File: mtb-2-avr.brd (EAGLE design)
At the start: 27 x 22 mm, 18 parts, among them IC1 MEGA8A-AU, Q1/2 14.745 MHz, Q2 14.745 MHz

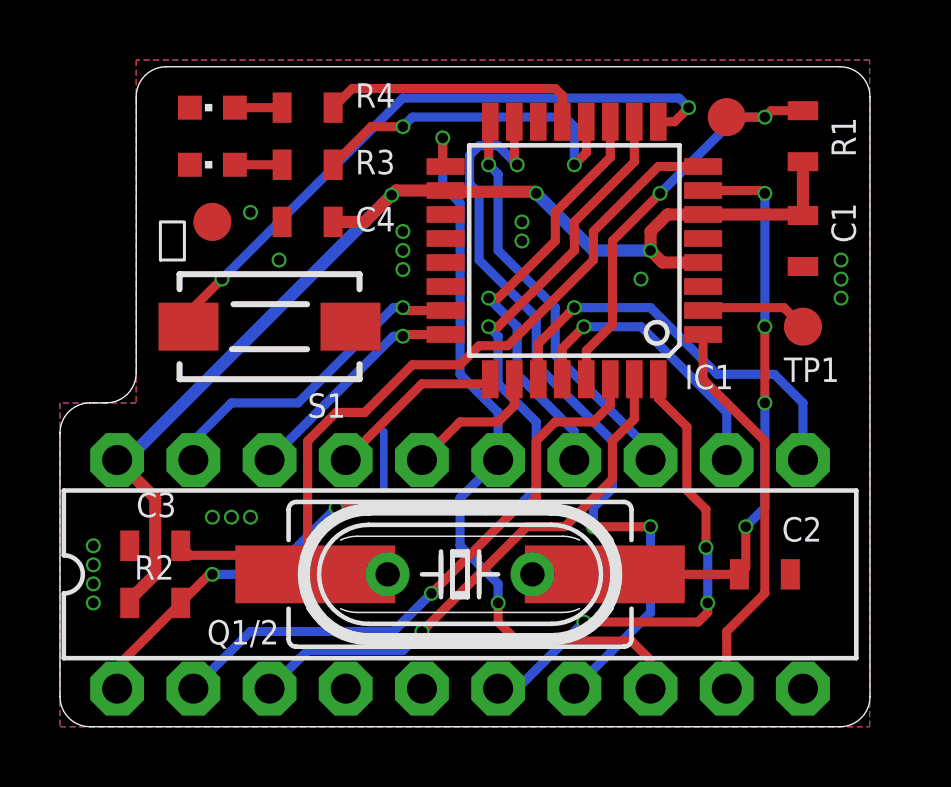
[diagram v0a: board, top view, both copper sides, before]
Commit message: Add pull-up on TX_OE.
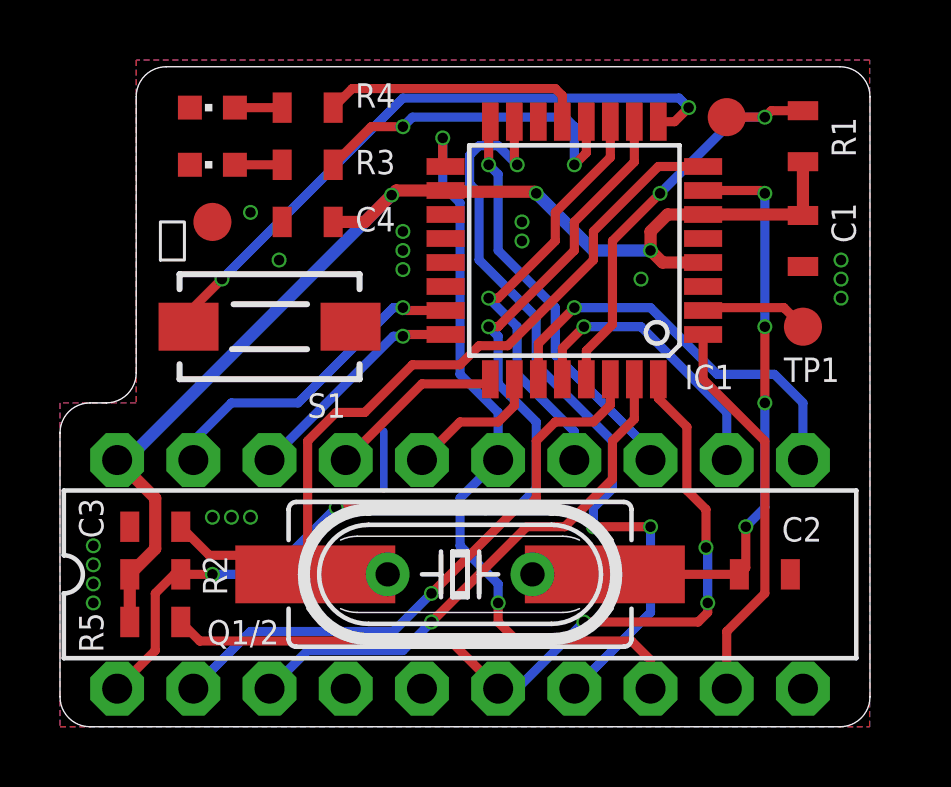
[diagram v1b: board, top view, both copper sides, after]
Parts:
- added R5: 100k, rcl:R0603
- moved R2 0.95 mm to (3.17, 5.08)
- moved C3 0.64 mm to (3.17, 6.67)
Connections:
- net TX_OE: now also R5.1
- net VCC: now also R5.2
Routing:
- net TX_OE: track 16.5 -> 28.0 mm
- net !SHIFT_OE: track 32.2 -> 32.9 mm
- net VCC: track 40.0 -> 40.6 mm
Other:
- board text added: "v1.2 JH 2021"
- board text removed: "v1.1 JH 2021"
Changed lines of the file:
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@@
 <text x="6.985" y="18.0975" size="1.016" layer="22" rot="MR0" align="bottom-center">MTB-UNI
 v2 upgrade</text>
-<text x="24.4475" y="16.51" size="1.016" layer="22" rot="MR90" align="bottom-center">v1.1 JH 2021</text>
+<text x="24.4475" y="16.51" size="1.016" layer="22" rot="MR90" align="bottom-center">v1.2 JH 2021</text>
 <text x="24.765" y="2.54" size="1.27" layer="22" rot="MR90" align="center-left">⏚</text>
 <text x="17.145" y="2.54" size="1.27" layer="22" rot="MR90" align="center-left">MOSI</text>
@@
 <attribute name="VALUE" x="24.765" y="4.1275" size="0.8128" layer="27" rot="R180"/>
 </element>
-<element name="C3" library="rcl" package="C0603" value="22p" x="3.175" y="6.0325" smashed="yes">
-<attribute name="LCSC_PART" value="C1653" x="3.175" y="6.0325" size="1.778" layer="27" display="off"/>
-<attribute name="NAME" x="2.54" y="6.985" size="0.8128" layer="25"/>
-<attribute name="VALUE" x="4.445" y="5.715" size="0.8128" layer="27"/>
+<element name="C3" library="rcl" package="C0603" value="22p" x="3.175" y="6.6675" smashed="yes">
+<attribute name="LCSC_PART" value="C1653" x="3.175" y="6.6675" size="1.778" layer="27" display="off"/>
+<attribute name="NAME" x="0.635" y="7.62" size="0.8128" layer="25" rot="R270"/>
+<attribute name="VALUE" x="4.445" y="6.35" size="0.8128" layer="27"/>
 </element>
 <element name="C4" library="rcl" package="C0603" value="100n" x="8.255" y="16.8275" smashed="yes" rot="R180">
@@
 <attribute name="VALUE" x="6.985" y="17.145" size="0.8128" layer="27" rot="R180"/>
 </element>
-<element name="R2" library="rcl" package="R0603" value="10k" x="3.175" y="4.1275" smashed="yes" rot="R180">
-<attribute name="LCSC_PART" value="C25804" x="3.175" y="4.1275" size="1.778" layer="27" rot="R180" display="off"/>
-<attribute name="NAME" x="3.81" y="5.715" size="0.8128" layer="25" rot="R180"/>
-<attribute name="VALUE" x="1.905" y="4.445" size="0.8128" layer="27" rot="R180"/>
+<element name="R2" library="rcl" package="R0603" value="10k" x="3.175" y="5.08" smashed="yes" rot="R180">
+<attribute name="LCSC_PART" value="C25804" x="3.175" y="5.08" size="1.778" layer="27" rot="R180" display="off"/>
+<attribute name="NAME" x="4.7625" y="5.715" size="0.8128" layer="25" rot="R270"/>
+<attribute name="VALUE" x="1.905" y="5.3975" size="0.8128" layer="27" rot="R180"/>
 </element>
 <element name="R3" library="rcl" package="R0603" value="10k" x="8.255" y="18.7325" smashed="yes">
@@
 <attribute name="OC_NEWARK" value="unknown" x="13.335" y="5.08" size="1.778" layer="27" display="off"/>
 <attribute name="POPULARITY" value="49" x="13.335" y="5.08" size="1.778" layer="27" display="off"/>
-<attribute name="VALUE" x="8.255" y="1.143" size="1.27" layer="27" ratio="10"/>
+</element>
+<element name="R5" library="rcl" package="R0603" value="100k" x="3.175" y="3.4925" smashed="yes" rot="R180">
+<attribute name="LCSC_PART" value="C25803" x="3.175" y="3.4925" size="1.778" layer="27" rot="R180" display="off"/>
+<attribute name="NAME" x="0.635" y="3.81" size="0.8128" layer="25" rot="R270"/>
+<attribute name="VALUE" x="4.445" y="3.175" size="0.8128" layer="27"/>
 </element>
 </elements>
@@
 <wire x1="17.78" y1="15.875" x2="15.875" y2="17.78" width="0.4064" layer="16"/>
 <wire x1="19.685" y1="15.875" x2="17.78" y2="15.875" width="0.4064" layer="16"/>
-<wire x1="3.175" y1="5.08" x2="2.325" y2="4.23" width="0.4064" layer="1"/>
-<wire x1="2.325" y1="4.23" x2="2.325" y2="4.1275" width="0.4064" layer="1"/>
-<wire x1="3.175" y1="7.62" x2="3.175" y2="5.08" width="0.4064" layer="1"/>
+<wire x1="3.175" y1="5.93" x2="2.325" y2="5.08" width="0.4064" layer="1"/>
+<wire x1="3.175" y1="7.62" x2="3.175" y2="5.93" width="0.4064" layer="1"/>
 <wire x1="24.765" y1="18.835" x2="24.765" y2="17.0425" width="0.4064" layer="1"/>
 <via x="11.05480625" y="17.72230625" extent="1-16" drill="0.35"/>
@@
 <wire x1="9.105" y1="16.8275" x2="10.16" y2="16.8275" width="0.4064" layer="1"/>
 <wire x1="10.16" y1="16.8275" x2="11.05480625" y2="17.72230625" width="0.4064" layer="1"/>
+<contactref element="R5" pad="2"/>
+<wire x1="2.325" y1="3.4925" x2="2.325" y2="5.08" width="0.4064" layer="1"/>
 </signal>
 <signal name="RXD">
@@
 <wire x1="6.985" y1="1.27" x2="8.255" y2="2.54" width="0.3048" layer="16"/>
 <wire x1="8.255" y1="2.54" x2="11.43" y2="2.54" width="0.3048" layer="16"/>
-<wire x1="11.43" y1="2.54" x2="12.065" y2="3.175" width="0.3048" layer="16"/>
-<wire x1="15.5575" y1="6.6675" x2="12.065" y2="3.175" width="0.3048" layer="1"/>
-<via x="12.065" y="3.175" extent="1-16" drill="0.35"/>
+<wire x1="11.43" y1="2.54" x2="12.3825" y2="3.4925" width="0.3048" layer="16"/>
+<wire x1="15.5575" y1="6.6675" x2="12.3825" y2="3.4925" width="0.3048" layer="1"/>
+<via x="12.3825" y="3.4925" extent="1-16" drill="0.35"/>
 <wire x1="16.8275" y1="6.6675" x2="15.5575" y2="6.6675" width="0.3048" layer="1"/>
 </signal>
@@
 <wire x1="17.4625" y1="3.4925" x2="15.24" y2="1.27" width="0.3048" layer="16"/>
 <via x="17.4625" y="3.4925" extent="1-16" drill="0.35"/>
+<contactref element="R5" pad="1"/>
+<wire x1="14.605" y1="1.27" x2="13.0175" y2="2.8575" width="0.3048" layer="1"/>
+<wire x1="4.66" y1="2.8575" x2="4.025" y2="3.4925" width="0.3048" layer="1"/>
+<wire x1="13.0175" y1="2.8575" x2="4.66" y2="2.8575" width="0.3048" layer="1"/>
 </signal>
 <signal name="OUT_SET">
@@
 <wire x1="8.255" y1="5.334" x2="8.255" y2="9.525" width="0.3048" layer="1"/>
 <wire x1="11.7475" y1="12.065" x2="13.335" y2="12.065" width="0.3048" layer="1"/>
-<wire x1="4.3425" y1="5.715" x2="4.025" y2="6.0325" width="0.3048" layer="1"/>
-<wire x1="7.874" y1="5.715" x2="4.3425" y2="5.715" width="0.3048" layer="1"/>
+<wire x1="4.9775" y1="5.715" x2="4.025" y2="6.6675" width="0.3048" layer="1"/>
+<wire x1="7.874" y1="5.715" x2="4.9775" y2="5.715" width="0.3048" layer="1"/>
 <wire x1="21.4376" y1="18.675" x2="19.945" y2="18.675" width="0.3048" layer="1"/>
 <wire x1="19.945" y1="18.675" x2="17.78" y2="16.51" width="0.3048" layer="1"/>
@@
 <wire x1="14.1831" y1="7.3025" x2="9.2075" y2="7.3025" width="0.3048" layer="1"/>
 <wire x1="15.24" y1="7.3025" x2="14.1831" y2="7.3025" width="0.3048" layer="16"/>
-<wire x1="1.905" y1="1.27" x2="1.905" y2="2.0075" width="0.3048" layer="1"/>
-<wire x1="1.905" y1="2.0075" x2="4.025" y2="4.1275" width="0.3048" layer="1"/>
 <via x="9.2075" y="7.3025" extent="1-16" drill="0.35"/>
 <wire x1="9.2075" y1="7.3025" x2="6.985" y2="5.08" width="0.3048" layer="16"/>
 <wire x1="6.985" y1="5.08" x2="5.08" y2="5.08" width="0.3048" layer="16"/>
 <via x="5.08" y="5.08" extent="1-16" drill="0.35"/>
-<wire x1="5.08" y1="5.08" x2="4.9775" y2="5.08" width="0.3048" layer="1"/>
-<wire x1="4.9775" y1="5.08" x2="4.025" y2="4.1275" width="0.3048" layer="1"/>
+<wire x1="5.08" y1="5.08" x2="4.025" y2="5.08" width="0.3048" layer="1"/>
+<wire x1="1.905" y1="1.27" x2="3.175" y2="2.54" width="0.3048" layer="1"/>
+<wire x1="3.175" y1="2.54" x2="3.175" y2="4.445" width="0.3048" layer="1"/>
+<wire x1="3.175" y1="4.445" x2="3.81" y2="5.08" width="0.3048" layer="1"/>
+<wire x1="3.81" y1="5.08" x2="4.025" y2="5.08" width="0.3048" layer="1"/>
 </signal>
 <signal name="N$3">

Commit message: Minor tweaks of wire positions.
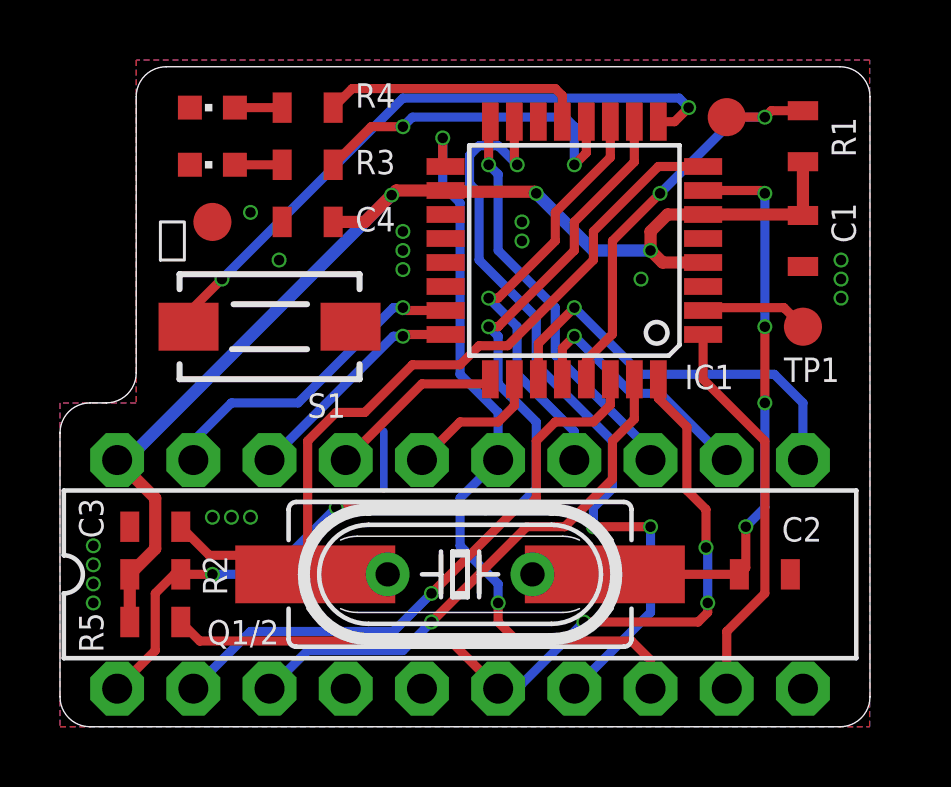
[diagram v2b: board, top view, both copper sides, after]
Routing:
- net SCL: track 9.58 -> 8.39 mm
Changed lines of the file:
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@@
 <wire x1="24.765" y1="8.89" x2="24.765" y2="10.795" width="0.3048" layer="16"/>
 <wire x1="24.765" y1="10.795" x2="23.8125" y2="11.7475" width="0.3048" layer="16"/>
-<wire x1="23.8125" y1="11.7475" x2="21.9075" y2="11.7475" width="0.3048" layer="16"/>
-<wire x1="21.9075" y1="11.7475" x2="19.685" y2="13.97" width="0.3048" layer="16"/>
-<wire x1="19.685" y1="13.97" x2="17.145" y2="13.97" width="0.3048" layer="16"/>
+<wire x1="23.8125" y1="11.7475" x2="19.3675" y2="11.7475" width="0.3048" layer="16"/>
+<wire x1="19.3675" y1="11.7475" x2="17.145" y2="13.97" width="0.3048" layer="16"/>
 <wire x1="15.945" y1="11.5824" x2="15.945" y2="12.77" width="0.3048" layer="1"/>
 <wire x1="15.945" y1="12.77" x2="17.145" y2="13.97" width="0.3048" layer="1"/>
@@
 <contactref element="IC1" pad="28"/>
 <wire x1="16.745" y1="11.5824" x2="16.745" y2="12.6175" width="0.3048" layer="1"/>
-<wire x1="16.745" y1="12.6175" x2="17.4625" y2="13.335" width="0.3048" layer="1"/>
-<wire x1="22.225" y1="8.89" x2="22.225" y2="10.4775" width="0.3048" layer="16"/>
-<wire x1="22.225" y1="10.4775" x2="19.3675" y2="13.335" width="0.3048" layer="16"/>
-<wire x1="19.3675" y1="13.335" x2="17.4625" y2="13.335" width="0.3048" layer="16"/>
-<via x="17.4625" y="13.335" extent="1-16" drill="0.35"/>
+<wire x1="16.745" y1="12.6175" x2="17.145" y2="13.0175" width="0.3048" layer="1"/>
+<via x="17.145" y="13.0175" extent="1-16" drill="0.35"/>
+<wire x1="17.145" y1="13.0175" x2="19.05" y2="11.1125" width="0.3048" layer="16"/>
+<wire x1="19.05" y1="11.1125" x2="20.0025" y2="11.1125" width="0.3048" layer="16"/>
+<wire x1="20.0025" y1="11.1125" x2="22.225" y2="8.89" width="0.3048" layer="16"/>
 </signal>
 <signal name="CRYST+">
@@
 <contactref element="IC1" pad="29"/>
 <contactref element="R1" pad="1"/>
-<wire x1="17.545" y1="11.5824" x2="17.545" y2="12.5349" width="0.3048" layer="1"/>
-<wire x1="18.415" y1="13.4049" x2="17.545" y2="12.5349" width="0.3048" layer="1"/>
+<wire x1="17.545" y1="11.5824" x2="17.545" y2="12.2174" width="0.3048" layer="1"/>
+<wire x1="18.415" y1="13.0874" x2="17.545" y2="12.2174" width="0.3048" layer="1"/>
 <wire x1="20.0025" y1="17.78" x2="18.415" y2="16.1925" width="0.3048" layer="1"/>
-<wire x1="18.415" y1="16.1925" x2="18.415" y2="13.4049" width="0.3048" layer="1"/>
+<wire x1="18.415" y1="16.1925" x2="18.415" y2="13.0874" width="0.3048" layer="1"/>
 <via x="20.0025" y="17.78" extent="1-16" drill="0.35"/>
 <wire x1="20.0025" y1="17.78" x2="22.5425" y2="20.32" width="0.3048" layer="16"/>

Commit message: Use ATmega328.
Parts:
- IC1: value MEGA8A-AU -> MEGA328A-AU
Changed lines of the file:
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@@
 </autorouter>
 <elements>
-<element name="IC1" library="atmel" library_urn="urn:adsk.eagle:library:105" package="TQFP32-08" package3d_urn="urn:adsk.eagle:package:4313/2" value="MEGA8A-AU" x="17.145" y="15.875" smashed="yes" rot="R180">
-<attribute name="LCSC_PART" value="C16190" x="17.145" y="15.875" size="1.778" layer="27" rot="R180" display="off"/>
+<element name="IC1" library="atmel" library_urn="urn:adsk.eagle:library:105" package="TQFP32-08" package3d_urn="urn:adsk.eagle:package:4313/2" value="MEGA328A-AU" x="17.145" y="15.875" smashed="yes" rot="R180">
+<attribute name="LCSC_PART" value="C14877" x="17.145" y="15.875" size="1.778" layer="27" rot="R180" display="off"/>
 <attribute name="MF" value="" x="-0.635" y="20.955" size="1.778" layer="27" rot="R180" display="off"/>
 <attribute name="MPN" value="ATMEGA8-16AU" x="-0.635" y="20.955" size="1.778" layer="27" rot="R180" display="off"/>

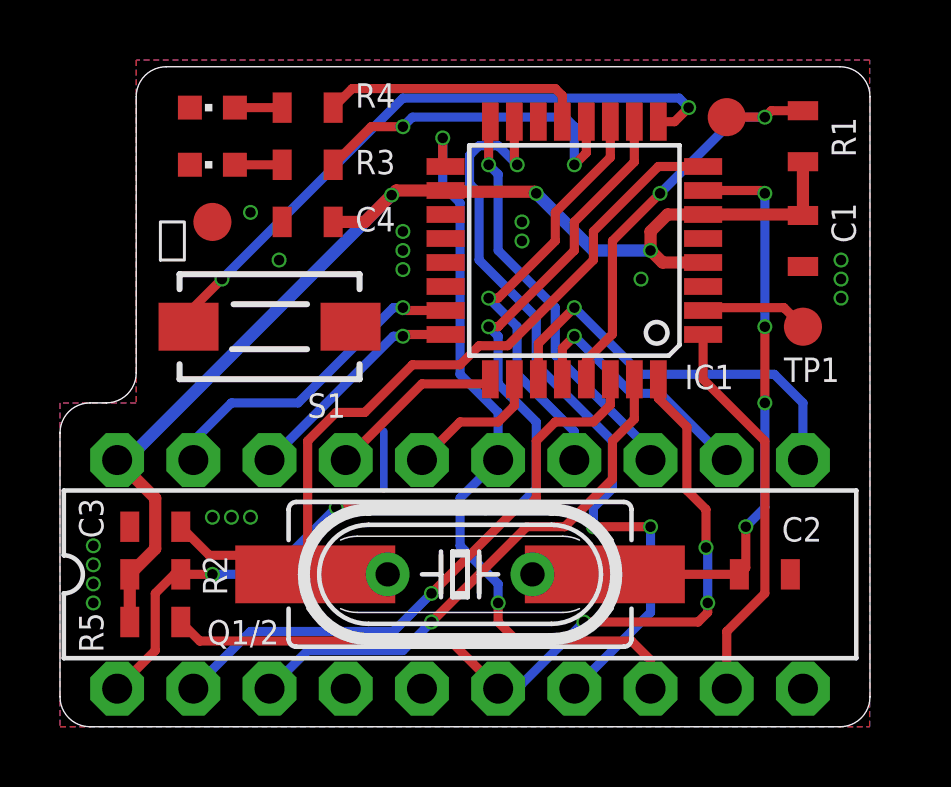
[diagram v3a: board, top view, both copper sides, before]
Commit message: Change outer dimensions to fit to MTB-TTL.
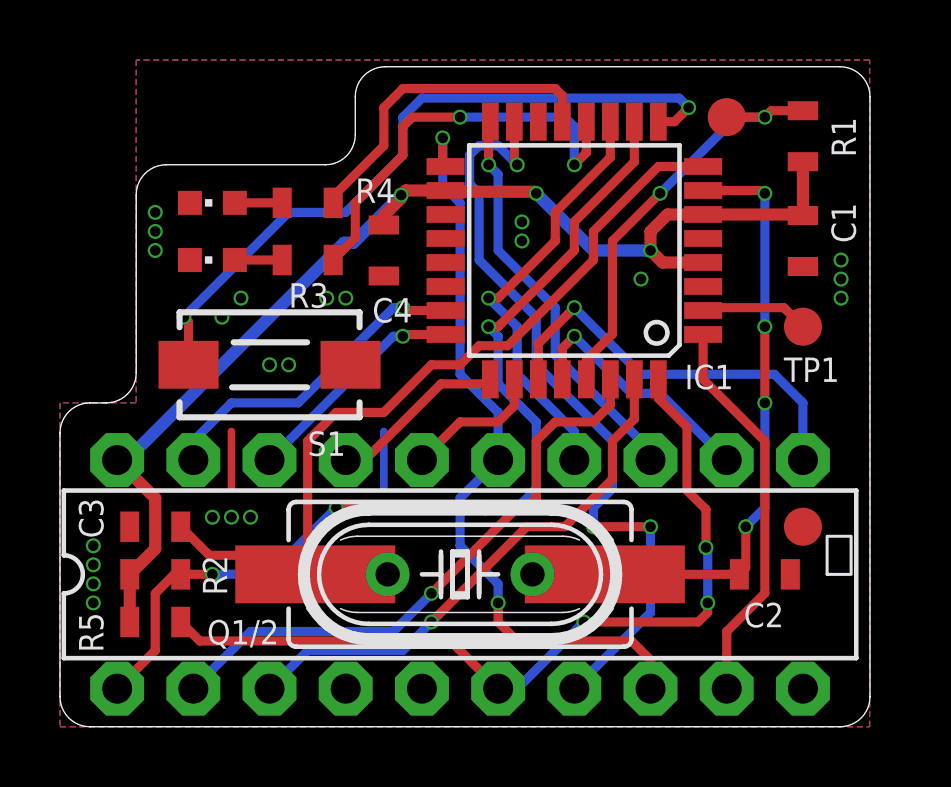
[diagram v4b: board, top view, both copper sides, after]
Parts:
- moved TP2 22.2 mm to (24.8, 6.67)
- moved LED1 3.18 mm to (5.08, 15.6)
- moved R3 3.18 mm to (8.26, 15.6)
- moved LED2 3.18 mm to (5.08, 17.5)
- moved R4 3.18 mm to (8.26, 17.5)
- moved C4 2.71 mm to (10.8, 15.9), turned to 270 degrees
- moved S1 1.27 mm to (6.99, 12.1)
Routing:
- net LED_GREEN: track 11.7 -> 14.3 mm
- net LED_BLUE: track 8.87 -> 11.1 mm
- net BTN: track 21.4 -> 23.6 mm
- net GND: track 1.90 -> 3.81 mm, vias 18 -> 22
- net VCC: track 40.6 -> 39.5 mm
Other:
- outline, holes or cut-outs redrawn
- board text added: "v1.3 JH 2021"
- board text removed: "v1.2 JH 2021"
